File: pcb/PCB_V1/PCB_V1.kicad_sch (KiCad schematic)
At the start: 13 parts, among them U101 TPS54202DDCR

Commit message: pcb: integrate reviewed parts and validate initial 100mm placement
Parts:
- L101: value 10uH / Isat >= 4.5A -> 10u SRP7050TA-100M; footprint Inductor_SMD:L_Coilcraft_XAL7050-XXX -> Inductor_SMD:L_Bourns_SRP7028A_7.3x6.6mm; LCSC (none) -> C2041441; MPN (none) -> SRP7050TA-100M; Manufacturer (none) -> Bourns
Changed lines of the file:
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@@
 	(title_block
 		(title "01 - Logic power / 12 V aux to 3.3 V")
-		(date "2026-09-27")
-		(rev "0.16-DRAFT")
+		(date "2026-09-28")
+		(rev "0.17-DRAFT")
 		(company "GrowBox controller")
 		(comment 1 "Engineering draft; startup, thermal and fault qualification pending")
@@
 			)
 		)
-		(property "Value" "10uH / Isat >= 4.5A"
+		(property "Value" "10u SRP7050TA-100M"
 			(at 130.81 58.42 90)
 			(show_name no)
@@
 			)
 		)
-		(property "Footprint" "Inductor_SMD:L_Coilcraft_XAL7050-XXX"
+		(property "Footprint" "Inductor_SMD:L_Bourns_SRP7028A_7.3x6.6mm"
 			(at 139.7 63.5 90)
 			(hide yes)
@@
 			)
 		)
-		(property "Datasheet" ""
+		(property "Datasheet" "https://www.bourns.com/docs/product-datasheets/srp7050ta.pdf"
 			(at 139.7 63.5 90)
 			(hide yes)
@@
 			)
 		)
+		(property "Manufacturer" "Bourns"
+			(at 139.7 63.5 90)
+			(hide yes)
+			(show_name no)
+			(do_not_autoplace no)
+			(effects
+				(font
+					(size 1 1)
+				)
+				(justify left)
+			)
+		)
+		(property "MPN" "SRP7050TA-100M"
+			(at 139.7 63.5 90)
+			(hide yes)
+			(show_name no)
+			(do_not_autoplace no)
+			(effects
+				(font
+					(size 1 1)
+				)
+				(justify left)
+			)
+		)
+		(property "LCSC" "C2041441"
+			(at 139.7 63.5 90)
+			(hide yes)
+			(show_name no)
+			(do_not_autoplace no)
+			(effects
+				(font
+					(size 1 1)
+				)
+				(justify left)
+			)
+		)

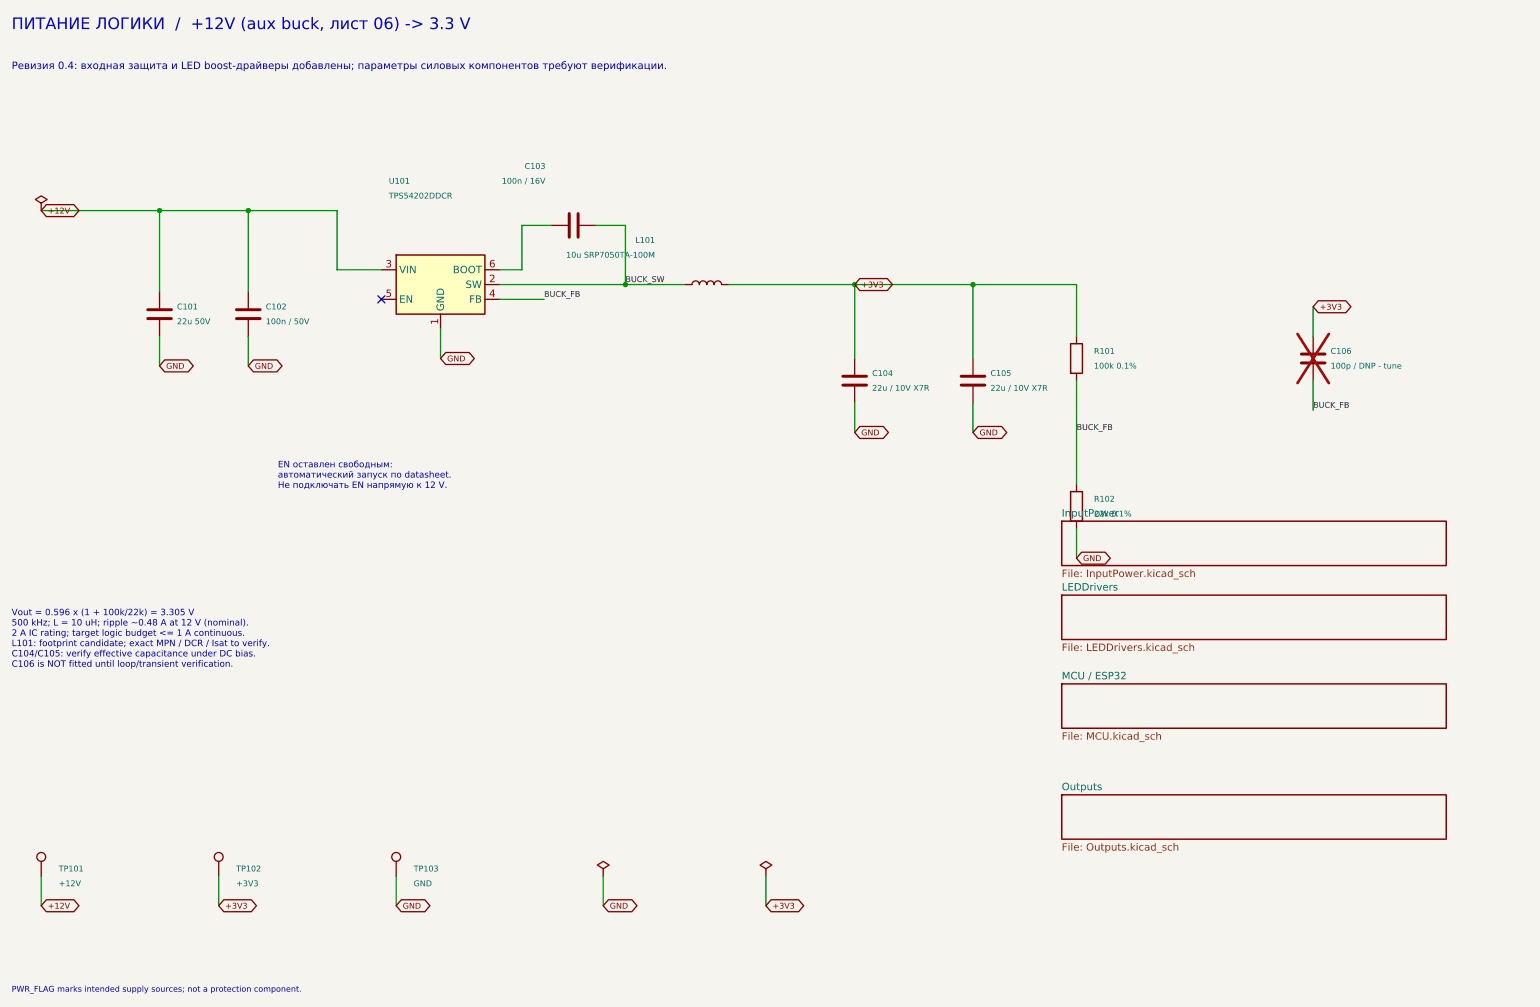
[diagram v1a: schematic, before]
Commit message: pcb: simplify passives and microSD circuitry for revision 0.18
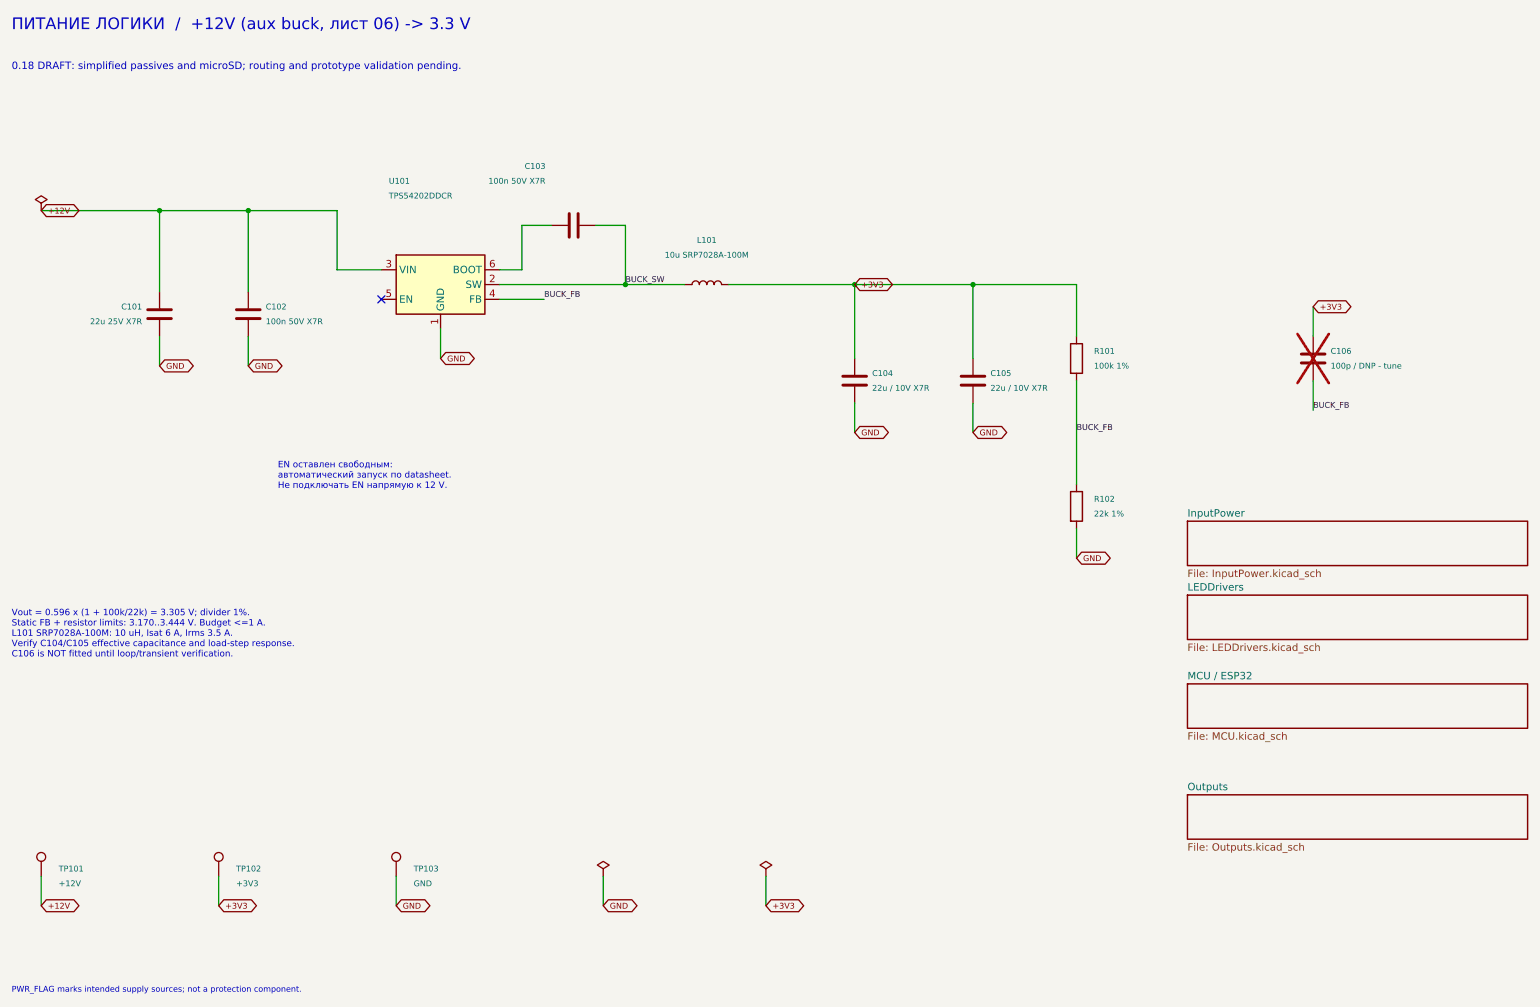
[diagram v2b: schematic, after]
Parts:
- C101: value 22u 50V -> 22u 25V X7R; LCSC (none) -> C309062; MPN (none) -> CL32B226KAJNNNE; Manufacturer (none) -> Samsung
- C102: value 100n / 50V -> 100n 50V X7R; LCSC (none) -> C1591; MPN (none) -> CL10B104KB8NNNC; Manufacturer (none) -> Samsung
- C103: value 100n / 16V -> 100n 50V X7R; LCSC (none) -> C1591; MPN (none) -> CL10B104KB8NNNC; Manufacturer (none) -> Samsung
- L101: value 10u SRP7050TA-100M -> 10u SRP7028A-100M; LCSC C2041441 -> C2687402; MPN SRP7050TA-100M -> SRP7028A-100M
- R101: value 100k 0.1% -> 100k 1%; LCSC (none) -> C25803; MPN (none) -> 0603WAF1003T5E; Manufacturer (none) -> UNI-ROYAL
- R102: value 22k 0.1% -> 22k 1%; LCSC (none) -> C31850; MPN (none) -> 0603WAF2202T5E; Manufacturer (none) -> UNI-ROYAL
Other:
- note added: "0.18 DRAFT: simplified passives and microSD; routing and prototype validation pending."
- note added: "Vout = 0.596 x (1 + 100k/22k) = 3.305 V; divider 1%. Static FB + resistor limits: 3.170..3.444 V. Budget <=1 A. L101 SRP7028A-100M: 10 uH, Isat 6 A, Irms 3.5 A. Verify C104/C105 effective capacitance and load-step response. C106 is NOT fitted until loop/transient verification."
- note removed: "Vout = 0.596 x (1 + 100k/22k) = 3.305 V 500 kHz; L = 10 uH; ripple ~0.48 A at 12 V (nominal). 2 A IC rating; target logic budget <= 1 A continuous. L101: footprint candidate; exact MPN / DCR / Isat to verify. C104/C105: verify effective capacitance under DC bias. C106 is NOT fitted until loop/transient verification."
- note removed: "Ревизия 0.4: входная защита и LED boost-драйверы добавлены; параметры силовых компонентов требуют верификации."
